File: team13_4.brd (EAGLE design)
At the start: 28 x 47 mm, 39 parts, among them J1 FTDI_DEVICE, M1 WIRELESS-NRF24L01, U1 ATMEGA328P_TQFP, U2 GY-521MPU6050, U3 MAX1595EUA33+, Y1 8MHz

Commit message: Remembered to command+s this time
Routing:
- net GND: track 33.7 -> 37.8 mm, vias 8 -> 10
- net N$1: track 10.0 -> 11.9 mm, vias 1 -> 2
- net VCC: track 26.1 -> 26.3 mm, vias 3 -> 4
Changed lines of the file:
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@@
 <setting verticaltext="up"/>
 </settings>
-<grid distance="39.3700787" unitdist="mil" unit="mil" style="lines" multiple="1" display="yes" altdistance="0.05" altunitdist="mm" altunit="mm"/>
+<grid distance="39.3700787" unitdist="mil" unit="mil" style="lines" multiple="1" display="yes" altdistance="0.005" altunitdist="mm" altunit="mm"/>
 <layers>
 <layer number="1" name="Top" color="4" fill="1" visible="yes" active="yes"/>
@@
 </class>
 </classes>
-<designrules name="oshpark-2layer-1">
+<designrules name="oshpark-2layer">
 <description language="en">&lt;b&gt;OSH Park Design Rules&lt;/b&gt;
 &lt;p&gt;
@@
 <wire x1="11.2268" y1="19.9898" x2="10.54" y2="20.6766" width="0.762" layer="1"/>
 <via x="11.2268" y="19.9898" extent="1-16" drill="0.35"/>
-<wire x1="12.57" y1="7.95" x2="12.57" y2="10.1316" width="0.508" layer="16"/>
 <wire x1="12.57" y1="10.1316" x2="12.573" y2="10.1346" width="0.508" layer="16"/>
 <polygon width="0.508" layer="16">
@@
 <vertex x="15" y="40"/>
 </polygon>
-<wire x1="10.02" y1="9.9174" x2="10.02" y2="8.52" width="0.508" layer="1"/>
-<wire x1="10.02" y1="8.52" x2="10" y2="8.5" width="0.508" layer="1"/>
-<wire x1="10" y1="5.3" x2="10" y2="5" width="0.762" layer="16"/>
 <wire x1="11.62" y1="9.9174" x2="11.62" y2="6.9662" width="0.508" layer="1"/>
 <wire x1="11.62" y1="6.9662" x2="11.6362" y2="6.95" width="0.508" layer="1"/>
@@
 <wire x1="11.6362" y1="6.95" x2="11.6862" y2="7" width="0.508" layer="16"/>
 <wire x1="11.6862" y1="7" x2="12" y2="7" width="0.508" layer="16"/>
-<wire x1="11.042" y1="5.2754" x2="9.6746" y2="5.2754" width="0.762" layer="1"/>
-<wire x1="9.6746" y1="5.2754" x2="9.5" y2="5.45" width="0.762" layer="1"/>
-<via x="9.5" y="5.45" extent="1-16" drill="0.35"/>
-<wire x1="9.5" y1="5.45" x2="9.65" y2="5.3" width="0.762" layer="16"/>
-<wire x1="9.65" y1="5.3" x2="10" y2="5.3" width="0.762" layer="16"/>
 <wire x1="13.64" y1="7.68" x2="13.64" y2="6.76" width="0.762" layer="1"/>
 <wire x1="13.64" y1="6.76" x2="14.7" y2="5.7" width="0.762" layer="1"/>
 <via x="14.7" y="5.7" extent="1-16" drill="0.35"/>
 <contactref element="U$1" pad="3"/>
-<wire x1="19.93" y1="7.67" x2="17.11" y2="7.99" width="0" layer="19" extent="1-16"/>
-<wire x1="10.02" y1="9.9174" x2="11.62" y2="9.9174" width="0" layer="19" extent="1-1"/>
+<wire x1="17.11" y1="7.99" x2="17.11" y2="6.76" width="0.762" layer="1"/>
+<wire x1="17.11" y1="6.76" x2="17.1" y2="6.75" width="0.762" layer="1"/>
+<via x="17.1" y="6.75" extent="1-16" drill="0.35"/>
+<wire x1="17.1" y1="6.75" x2="17" y2="6.85" width="0.762" layer="16"/>
+<wire x1="17" y1="6.85" x2="17" y2="7" width="0.762" layer="16"/>
+<via x="9.9" y="6.95" extent="1-16" drill="0.35"/>
+<wire x1="10.02" y1="9.9174" x2="9.9058" y2="9.8032" width="0.508" layer="1"/>
+<wire x1="9.9058" y1="9.8032" x2="9.9058" y2="9.1140625" width="0.508" layer="1"/>
+<wire x1="9.9058" y1="9.1140625" x2="9.9" y2="9.1082625" width="0.508" layer="1"/>
+<wire x1="9.9" y1="9.1082625" x2="9.9" y2="6.95" width="0.508" layer="1"/>
+<wire x1="11.042" y1="5.2754" x2="9.7246" y2="5.2754" width="0.762" layer="1"/>
+<wire x1="9.7246" y1="5.2754" x2="9.7" y2="5.3" width="0.762" layer="1"/>
+<via x="9.7" y="5.3" extent="1-16" drill="0.35"/>
+<wire x1="9.7" y1="5.3" x2="10" y2="5" width="0.762" layer="16"/>
+<wire x1="19.93" y1="7.67" x2="18.33" y2="7.67" width="0.3048" layer="16"/>
+<wire x1="18.33" y1="7.67" x2="18" y2="8" width="0.3048" layer="16"/>
+<wire x1="18" y1="8" x2="17.5" y2="8.5" width="0.3048" layer="16"/>
+<wire x1="17.5" y1="8.5" x2="17.5" y2="9.55" width="0.3048" layer="16"/>
 </signal>
 <signal name="IMU_INT">
@@
 <wire x1="15.1638" y1="4.4196" x2="15.1638" y2="3.5156" width="0.4826" layer="16"/>
 <wire x1="15.1638" y1="3.5156" x2="15.1744" y2="3.505" width="0.4826" layer="16"/>
-<wire x1="10.87" y1="7.95" x2="10" y2="7.08" width="0.762" layer="16"/>
-<wire x1="10" y1="7.08" x2="10" y2="7" width="0.762" layer="16"/>
-<via x="10" y="7" extent="1-16" drill="0.35"/>
-<wire x1="9.15" y1="8.15" x2="10" y2="7.3" width="0.762" layer="16"/>
-<wire x1="10" y1="7.3" x2="10" y2="7.08" width="0.762" layer="16"/>
 <polygon width="0.3048" layer="1">
 <vertex x="9" y="40"/>
@@
 <wire x1="3.89" y1="11.51" x2="2.49" y2="11.51" width="0.762" layer="1"/>
 <wire x1="2.49" y1="11.51" x2="2" y2="12" width="0.762" layer="1"/>
+<via x="10.8" y="6.85" extent="1-16" drill="0.35"/>
+<wire x1="10.87" y1="7.95" x2="10.87" y2="7.3652375" width="0.762" layer="16"/>
+<wire x1="10.87" y1="7.3652375" x2="10.8008" y2="7.2960375" width="0.762" layer="16"/>
+<wire x1="10.8008" y1="7.2960375" x2="10.8008" y2="6.8508" width="0.762" layer="16"/>
+<wire x1="10.8008" y1="6.8508" x2="10.8" y2="6.85" width="0.762" layer="16"/>
+<wire x1="10.8" y1="6.85" x2="10.8008" y2="6.8508" width="0.762" layer="1"/>
+<wire x1="10.8008" y1="6.8508" x2="10.8008" y2="7" width="0.762" layer="1"/>
+<wire x1="9.15" y1="8.15" x2="9.15" y2="7.55" width="0.762" layer="16"/>
+<wire x1="9.15" y1="7.55" x2="8.4" y2="6.8" width="0.762" layer="16"/>
+<via x="8.4" y="6.8" extent="1-16" drill="0.35"/>
 </signal>
 <signal name="FTDI_TX">
@@
 <wire x1="5.286" y1="12.814" x2="5.5118" y2="12.5882" width="0.3048" layer="16"/>
 <wire x1="5.5118" y1="10.2722875" x2="5.5118" y2="12.5882" width="0.3048" layer="16"/>
-<wire x1="7.46" y1="8.35" x2="5.5377125" y2="10.2722875" width="0.3048" layer="16"/>
+<wire x1="7.46" y1="8.35" x2="6.58" y2="9.23" width="0.3048" layer="16"/>
+<wire x1="6.58" y1="9.23" x2="5.5377125" y2="10.2722875" width="0.3048" layer="16"/>
 <wire x1="5.5377125" y1="10.2722875" x2="5.5118" y2="10.2722875" width="0.3048" layer="16"/>
 <wire x1="7.46" y1="8.51" x2="7.46" y2="8.35" width="0.3048" layer="16"/>
@@
 <wire x1="7.81" y1="8.51" x2="7.46" y2="8.51" width="0.3048" layer="16"/>
 <contactref element="U$1" pad="1"/>
-<wire x1="7.81" y1="8.51" x2="8.01" y2="7.99" width="0" layer="19" extent="1-16"/>
+<wire x1="8.01" y1="7.99" x2="6.77" y2="9.23" width="0.3048" layer="1"/>
+<wire x1="6.77" y1="9.23" x2="6.58" y2="9.23" width="0.3048" layer="1"/>
+<via x="6.58" y="9.23" extent="1-16" drill="0.35"/>
 </signal>
 <signal name="PWM2">
@@
 <contactref element="U1" pad="8"/>
 <contactref element="Y1" pad="3"/>
-<wire x1="14.84" y1="7.68" x2="14.52899375" y2="7.99100625" width="0.508" layer="1"/>
-<wire x1="14.52899375" y1="7.99100625" x2="14.52899375" y2="8.56135625" width="0.508" layer="1"/>
-<wire x1="14.52899375" y1="8.56135625" x2="14.045175" y2="9.045175" width="0.508" layer="1"/>
-<wire x1="14.045175" y1="9.045175" x2="14.045175" y2="9.892225" width="0.508" layer="1"/>
-<wire x1="14.045175" y1="9.892225" x2="14.02" y2="9.9174" width="0.508" layer="1"/>
+<wire x1="14.84" y1="7.68" x2="14.535" y2="7.985" width="0.508" layer="1"/>
+<wire x1="14.535" y1="7.985" x2="14.535" y2="8.55535" width="0.508" layer="1"/>
+<wire x1="14.02" y1="9.07035" x2="14.02" y2="9.9174" width="0.508" layer="1"/>
+<wire x1="14.535" y1="8.55535" x2="14.02" y2="9.07035" width="0.508" layer="1"/>
 </signal>
 <signal name="XTAL1">

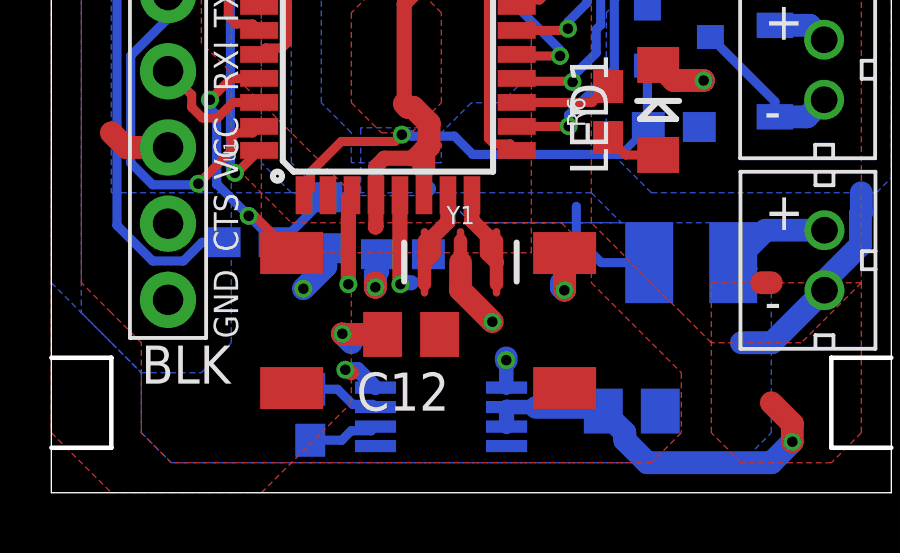
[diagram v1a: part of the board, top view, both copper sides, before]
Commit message: Adjusted pushbutton and nearby components
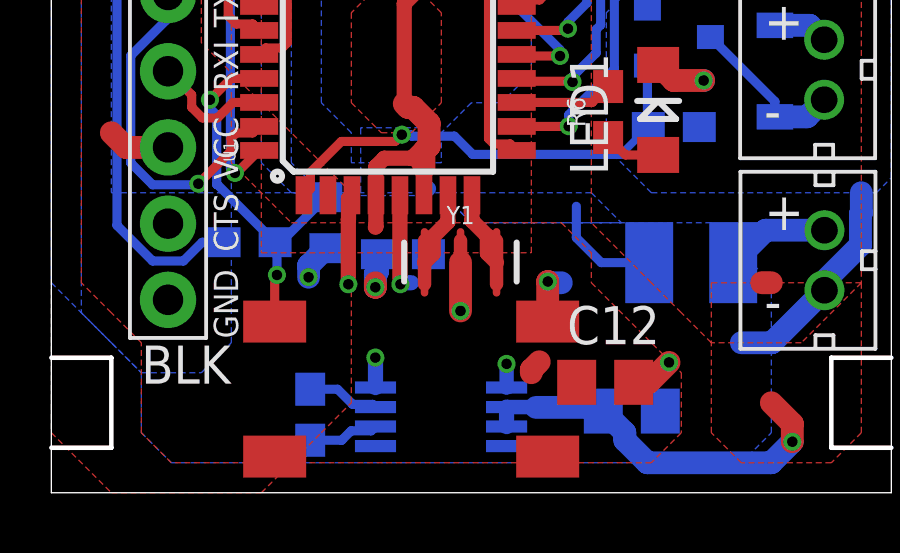
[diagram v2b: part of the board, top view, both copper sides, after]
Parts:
- moved C12 6.66 mm to (18.5, 3.68), turned to 0 degrees
- moved U$1 2.35 mm to (7.45, 5.71)
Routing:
- net GND: track 37.8 -> 36.9 mm
- net N$1: track 11.9 -> 12.7 mm
- net VCC: track 26.3 -> 25.6 mm
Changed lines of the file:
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@@
 <attribute name="SPICEPREFIX" value="C" x="6.61" y="8.35" size="1.778" layer="28" rot="MR0" display="off"/>
 </element>
-<element name="C12" library="rcl" library_urn="urn:adsk.eagle:library:334" package="C0805" package3d_urn="urn:adsk.eagle:package:23617/2" value="1uF" x="11.992" y="5.2754" rot="R180">
-<attribute name="SPICEPREFIX" value="C" x="11.992" y="5.2754" size="1.778" layer="27" rot="R180" display="off"/>
+<element name="C12" library="rcl" library_urn="urn:adsk.eagle:library:334" package="C0805" package3d_urn="urn:adsk.eagle:package:23617/2" value="1uF" x="18.462" y="3.6804">
+<attribute name="SPICEPREFIX" value="C" x="18.462" y="3.6804" size="1.778" layer="27" display="off"/>
 </element>
 <element name="C13" library="rcl" library_urn="urn:adsk.eagle:library:334" package="C1210" package3d_urn="urn:adsk.eagle:package:23619/2" value="100uF" x="21.33" y="7.67" rot="MR180">
@@
 <attribute name="SPICEPREFIX" value="R" x="11.3932" y="23.351" size="1.778" layer="27" display="off"/>
 </element>
-<element name="U$1" library="E-Switch" package="LL3301NF065QG" value="LL3301NF065QG" x="8.01" y="7.99"/>
+<element name="U$1" library="E-Switch" package="LL3301NF065QG" value="LL3301NF065QG" x="7.445" y="5.705"/>
 <element name="U$10" library="quad" package="MINI2-F3-B" value="DB2W40300L" x="23.58" y="22.53" rot="MR0"/>
 <element name="U$11" library="quad" package="JST_CONNECTOR_FEMALE" value="JST_CONNECTOR_FEMALE" x="25.68" y="22.6"/>
@@
 <wire x1="11.6362" y1="6.95" x2="11.6862" y2="7" width="0.508" layer="16"/>
 <wire x1="11.6862" y1="7" x2="12" y2="7" width="0.508" layer="16"/>
-<wire x1="13.64" y1="7.68" x2="13.64" y2="6.76" width="0.762" layer="1"/>
-<wire x1="13.64" y1="6.76" x2="14.7" y2="5.7" width="0.762" layer="1"/>
-<via x="14.7" y="5.7" extent="1-16" drill="0.35"/>
 <contactref element="U$1" pad="3"/>
-<wire x1="17.11" y1="7.99" x2="17.11" y2="6.76" width="0.762" layer="1"/>
-<wire x1="17.11" y1="6.76" x2="17.1" y2="6.75" width="0.762" layer="1"/>
-<via x="17.1" y="6.75" extent="1-16" drill="0.35"/>
-<wire x1="17.1" y1="6.75" x2="17" y2="6.85" width="0.762" layer="16"/>
-<wire x1="17" y1="6.85" x2="17" y2="7" width="0.762" layer="16"/>
 <via x="9.9" y="6.95" extent="1-16" drill="0.35"/>
 <wire x1="10.02" y1="9.9174" x2="9.9058" y2="9.8032" width="0.508" layer="1"/>
@@
 <wire x1="9.9058" y1="9.1140625" x2="9.9" y2="9.1082625" width="0.508" layer="1"/>
 <wire x1="9.9" y1="9.1082625" x2="9.9" y2="6.95" width="0.508" layer="1"/>
-<wire x1="11.042" y1="5.2754" x2="9.7246" y2="5.2754" width="0.762" layer="1"/>
-<wire x1="9.7246" y1="5.2754" x2="9.7" y2="5.3" width="0.762" layer="1"/>
-<via x="9.7" y="5.3" extent="1-16" drill="0.35"/>
-<wire x1="9.7" y1="5.3" x2="10" y2="5" width="0.762" layer="16"/>
 <wire x1="19.93" y1="7.67" x2="18.33" y2="7.67" width="0.3048" layer="16"/>
-<wire x1="18.33" y1="7.67" x2="18" y2="8" width="0.3048" layer="16"/>
-<wire x1="18" y1="8" x2="17.5" y2="8.5" width="0.3048" layer="16"/>
+<wire x1="18.33" y1="7.67" x2="17.5" y2="8.5" width="0.3048" layer="16"/>
 <wire x1="17.5" y1="8.5" x2="17.5" y2="9.55" width="0.3048" layer="16"/>
+<wire x1="16.545" y1="5.705" x2="16.545" y2="7.035" width="0.762" layer="1"/>
+<wire x1="16.545" y1="7.035" x2="16.55" y2="7.04" width="0.762" layer="1"/>
+<via x="16.55" y="7.04" extent="1-16" drill="0.35"/>
+<wire x1="16.55" y1="7.04" x2="16.59" y2="7" width="0.762" layer="16"/>
+<wire x1="16.59" y1="7" x2="17" y2="7" width="0.762" layer="16"/>
+<wire x1="19.412" y1="3.6804" x2="19.9254" y2="3.6804" width="0.762" layer="1"/>
+<wire x1="19.9254" y1="3.6804" x2="20.59" y2="4.345" width="0.762" layer="1"/>
+<via x="20.59" y="4.345" extent="1-16" drill="0.35"/>
+<wire x1="13.64" y1="7.68" x2="13.64" y2="6.06" width="0.762" layer="1"/>
+<via x="13.64" y="6.06" extent="1-16" drill="0.35"/>
 </signal>
 <signal name="IMU_INT">
@@
 <wire x1="13.2334" y1="19.7104" x2="13.2334" y2="18.516" width="0.508" layer="1"/>
 <wire x1="13.2334" y1="18.516" x2="13.22" y2="18.5026" width="0.508" layer="1"/>
-<wire x1="15.1638" y1="4.4958" x2="15.1638" y2="4.4196" width="0.762" layer="16"/>
-<via x="15.1638" y="4.4196" extent="1-16" drill="0.35"/>
 <wire x1="13.22" y1="18.5026" x2="13.1058" y2="18.3884" width="0.508" layer="1"/>
 <wire x1="12.4686" y1="12.26019375" x2="12.4686" y2="11.61020625" width="0.508" layer="1"/>
@@
 <wire x1="12.0616" y1="12.8468" x2="11.88199375" y2="12.8468" width="0.762" layer="1"/>
 <wire x1="11.88199375" y1="12.8468" x2="11.763" y2="12.96579375" width="0.762" layer="1"/>
-<wire x1="15.1744" y1="4.4852" x2="15.1638" y2="4.4958" width="0.508" layer="16"/>
 <polygon width="0.3048" layer="1">
 <vertex x="12" y="17"/>
@@
 <vertex x="0" y="42"/>
 </polygon>
-<wire x1="15.1638" y1="4.4196" x2="15.1638" y2="3.5156" width="0.4826" layer="16"/>
-<wire x1="15.1638" y1="3.5156" x2="15.1744" y2="3.505" width="0.4826" layer="16"/>
 <polygon width="0.3048" layer="1">
 <vertex x="9" y="40"/>
@@
 <vertex x="9" y="27"/>
 </polygon>
-<wire x1="10.8056" y1="3.505" x2="10.2106" y2="4.1" width="0.508" layer="16"/>
-<wire x1="10.2106" y1="4.1" x2="9.8" y2="4.1" width="0.508" layer="16"/>
-<via x="9.8" y="4.1" extent="1-16" drill="0.35"/>
-<wire x1="9.8" y1="4.1" x2="9.9" y2="4.1" width="0.508" layer="1"/>
-<wire x1="9.9" y1="4.1" x2="10" y2="4" width="0.508" layer="1"/>
 <wire x1="10.82" y1="9.9174" x2="10.82" y2="8.87" width="0.508" layer="1"/>
 <wire x1="10.82" y1="8.87" x2="10.8" y2="8.85" width="0.508" layer="1"/>
@@
 <wire x1="10.8" y1="6.85" x2="10.8008" y2="6.8508" width="0.762" layer="1"/>
 <wire x1="10.8008" y1="6.8508" x2="10.8008" y2="7" width="0.762" layer="1"/>
-<wire x1="9.15" y1="8.15" x2="9.15" y2="7.55" width="0.762" layer="16"/>
-<wire x1="9.15" y1="7.55" x2="8.4" y2="6.8" width="0.762" layer="16"/>
-<via x="8.4" y="6.8" extent="1-16" drill="0.35"/>
+<via x="8.575" y="7.185" extent="1-16" drill="0.35"/>
+<wire x1="9.15" y1="8.15" x2="8.575" y2="7.575" width="0.762" layer="16"/>
+<wire x1="8.575" y1="7.575" x2="8.575" y2="7.185" width="0.762" layer="16"/>
+<wire x1="16.265" y1="4.365" x2="16" y2="4.1" width="0.762" layer="1"/>
+<wire x1="16" y1="4.1" x2="16" y2="4" width="0.762" layer="1"/>
+<wire x1="10.8056" y1="3.505" x2="10.8056" y2="4.4994" width="0.508" layer="16"/>
+<wire x1="10.8056" y1="4.4994" x2="10.8" y2="4.505" width="0.508" layer="16"/>
+<via x="10.8" y="4.505" extent="1-16" drill="0.35"/>
+<wire x1="15.1744" y1="3.505" x2="15.1744" y2="4.2944" width="0.4826" layer="16"/>
+<wire x1="15.1744" y1="4.2944" x2="15.175" y2="4.295" width="0.4826" layer="16"/>
+<via x="15.175" y="4.295" extent="1-16" drill="0.35"/>
 </signal>
 <signal name="FTDI_TX">
@@
 <wire x1="5.286" y1="12.814" x2="5.5118" y2="12.5882" width="0.3048" layer="16"/>
 <wire x1="5.5118" y1="10.2722875" x2="5.5118" y2="12.5882" width="0.3048" layer="16"/>
-<wire x1="7.46" y1="8.35" x2="6.58" y2="9.23" width="0.3048" layer="16"/>
-<wire x1="6.58" y1="9.23" x2="5.5377125" y2="10.2722875" width="0.3048" layer="16"/>
+<wire x1="7.46" y1="8.35" x2="5.5377125" y2="10.2722875" width="0.3048" layer="16"/>
 <wire x1="5.5377125" y1="10.2722875" x2="5.5118" y2="10.2722875" width="0.3048" layer="16"/>
 <wire x1="7.46" y1="8.51" x2="7.46" y2="8.35" width="0.3048" layer="16"/>
@@
 <wire x1="7.81" y1="8.51" x2="7.46" y2="8.51" width="0.3048" layer="16"/>
 <contactref element="U$1" pad="1"/>
-<wire x1="8.01" y1="7.99" x2="6.77" y2="9.23" width="0.3048" layer="1"/>
-<wire x1="6.77" y1="9.23" x2="6.58" y2="9.23" width="0.3048" layer="1"/>
-<via x="6.58" y="9.23" extent="1-16" drill="0.35"/>
+<via x="7.52" y="7.26" extent="1-16" drill="0.35"/>
+<wire x1="7.52" y1="7.26" x2="7.52" y2="8.29" width="0.3048" layer="16"/>
+<wire x1="7.52" y1="8.29" x2="7.46" y2="8.35" width="0.3048" layer="16"/>
+<wire x1="7.445" y1="5.705" x2="7.445" y2="7.185" width="0.3048" layer="1"/>
+<wire x1="7.445" y1="7.185" x2="7.52" y2="7.26" width="0.3048" layer="1"/>
 </signal>
 <signal name="PWM2">

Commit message: lkdjhflcsnrhglsefhglwkfghulicurhngihxfhwleurqh;bk
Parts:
- moved C5 2.79 mm to (11.3, 36.4)
- moved C6 2.79 mm to (13.6, 36.4)
- moved J1 2.11 mm to (3.40, 14.8)
- moved M1 1.66 mm to (11.9, 31.8), flipped to the top
- moved U2 1.35 mm to (15.6, 30.9), flipped to the bottom, turned to 180 degrees
- moved U$11 1.00 mm to (24.7, 22.6)
- moved U$3 1.00 mm to (24.7, 31.4)
- moved U$7 1.00 mm to (24.8, 14.1)
- moved U$19 0.95 mm to (24.8, 7.84)
- moved U$6 0.86 mm to (23.3, 14.0)
- moved R9 0.85 mm to (12.2, 23.4)
- moved C2 0.83 mm to (12.2, 21.1)
- moved U$15 0.82 mm to (24.8, 39.1)
- moved U$4 0.47 mm to (23.2, 31.5)
- moved U$10 0.43 mm to (23.2, 22.5)
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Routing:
- net IMU_INT: track 13.1 -> 33.4 mm
- net IMU_SCL: track 21.8 -> 15.8 mm, vias 0 -> 1
- net GND: track 36.9 -> 31.5 mm, vias 10 -> 9
- net NRF_SCK: track 32.9 -> 37.5 mm
- net NRF_MOSI: track 33.3 -> 28.8 mm
- net NRF_CE: track 39.5 -> 36.1 mm
- net PWM4: track 34.5 -> 37.2 mm
- net FTDI_RX: track 4.14 -> 6.39 mm
- net VIN: track 25.9 -> 23.7 mm
- net FTDI_TX: track 11.8 -> 9.67 mm
- net NRF_CSN: track 34.1 -> 32.2 mm
- net VCC: track 25.6 -> 23.8 mm
- net IMU_SDA: track 18.9 -> 17.5 mm, vias 0 -> 1
- net FTDI_DTR: track 15.2 -> 13.9 mm
- net N$1: track 12.7 -> 13.4 mm
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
